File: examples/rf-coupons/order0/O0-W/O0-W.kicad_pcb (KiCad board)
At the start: 4 copper layers, 105.1 x 71.6 mm, 37 parts, among them X16 Anchor, X18 Anchor, X29 Anchor, X32 Anchor, X35 Anchor

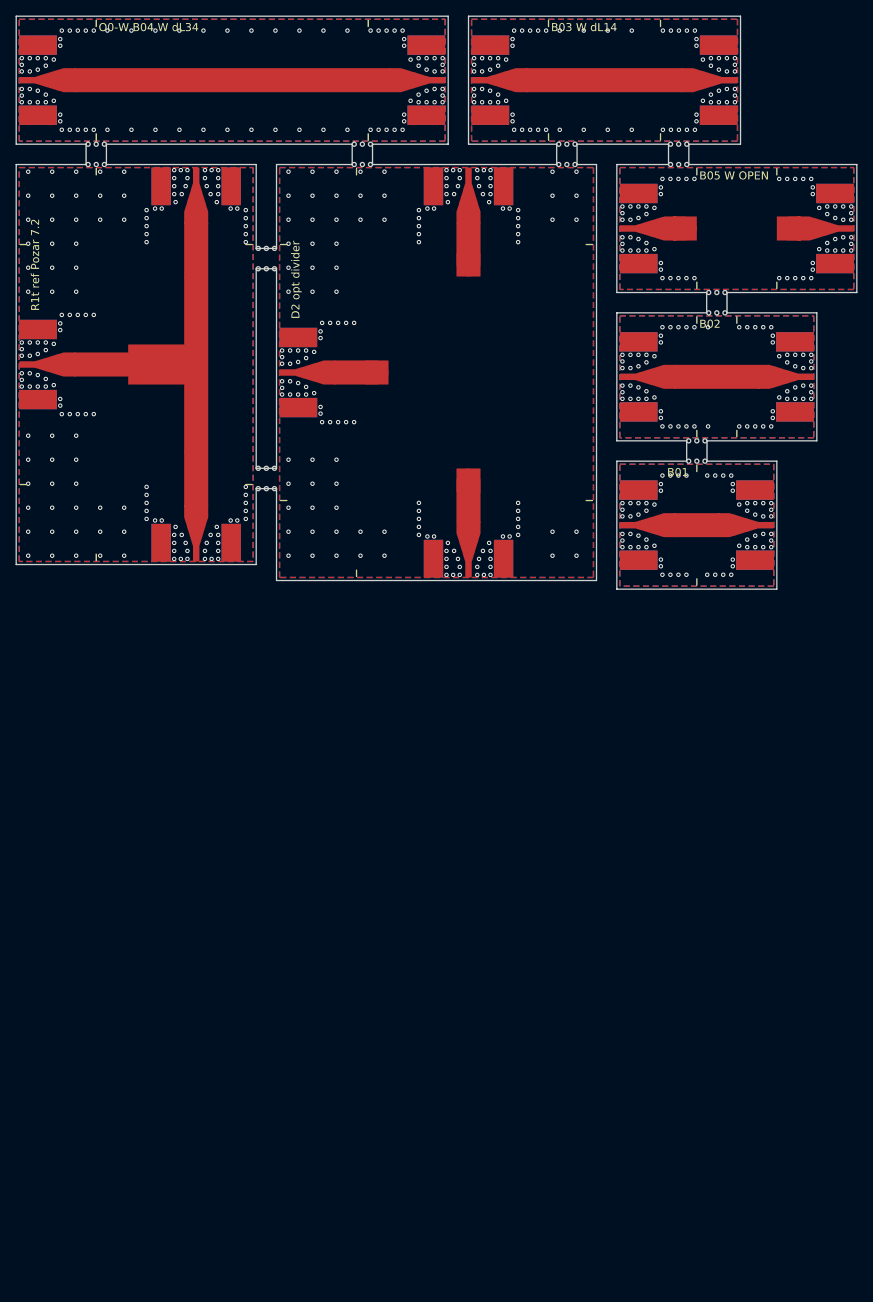
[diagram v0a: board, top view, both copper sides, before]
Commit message: Order 0: the uploads and predictions regenerated after the review
examples/rf-coupons/order0: generated from 73fe6527 (the tag carries it); KiCad
DRC under OSH Park's 4-layer rules 0 violations / 0 unconnected on all three.
`yapnr fab check` (oshpark-4l, oshpark-4l-fr408hr): O0-M 0 errors; O0-W and
O0-D stop on FAB-PLACEHOLDER until D2 and D1 are in (by design); warnings as
before (NPTH in the merged drill file; 1.511 mm of published layers):

- O0-M 120.1 x 144.3 mm, 26.9 sq in, 33 SMAs per copy, 32 tabs;
- O0-W 57.5 x 131.2 mm, 11.7 sq in, 16 SMAs, 15 tabs;
- O0-D 90.6 x 51.5 mm, 7.2 sq in, 12 SMAs, 9 tabs (A20 added).

Every stick has two or more tabs, all on edges without a launch; no plane via
under a silkscreen glyph; no mask web under 0.1 mm; the QR decodes from the
silkscreen render.

Predictions: the coupons on FR408HR and EM528 with the review's roughness
prior, the junction-corrected ring and stub (A12 notch 5.500 GHz FR408HR,
5.388 GHz EM528; A11 1.924 / 5.793 GHz), scalars.json and lines.csv. Boards A
and B regenerated (mask-opening anchors only; DRC unchanged).

docs/rf/order0: sizes and costs, R1/R1t as drawn, the renormalization to the
solver's port impedance (review H3), the C-pad method (M3), the loss basis
(M4), the scalars (L1), the sha256 rule (F9), the connector-fit pre-check, the
mask web note (L2), and the D1/D2 pages with the board around each window.

Co-Authored-By: Claude Opus 5.5 <noreply@anthropic.com>
Claude-Session: https://claude.ai/code/session_01NY8rMuBH8hTFjkoZyuqNZ7
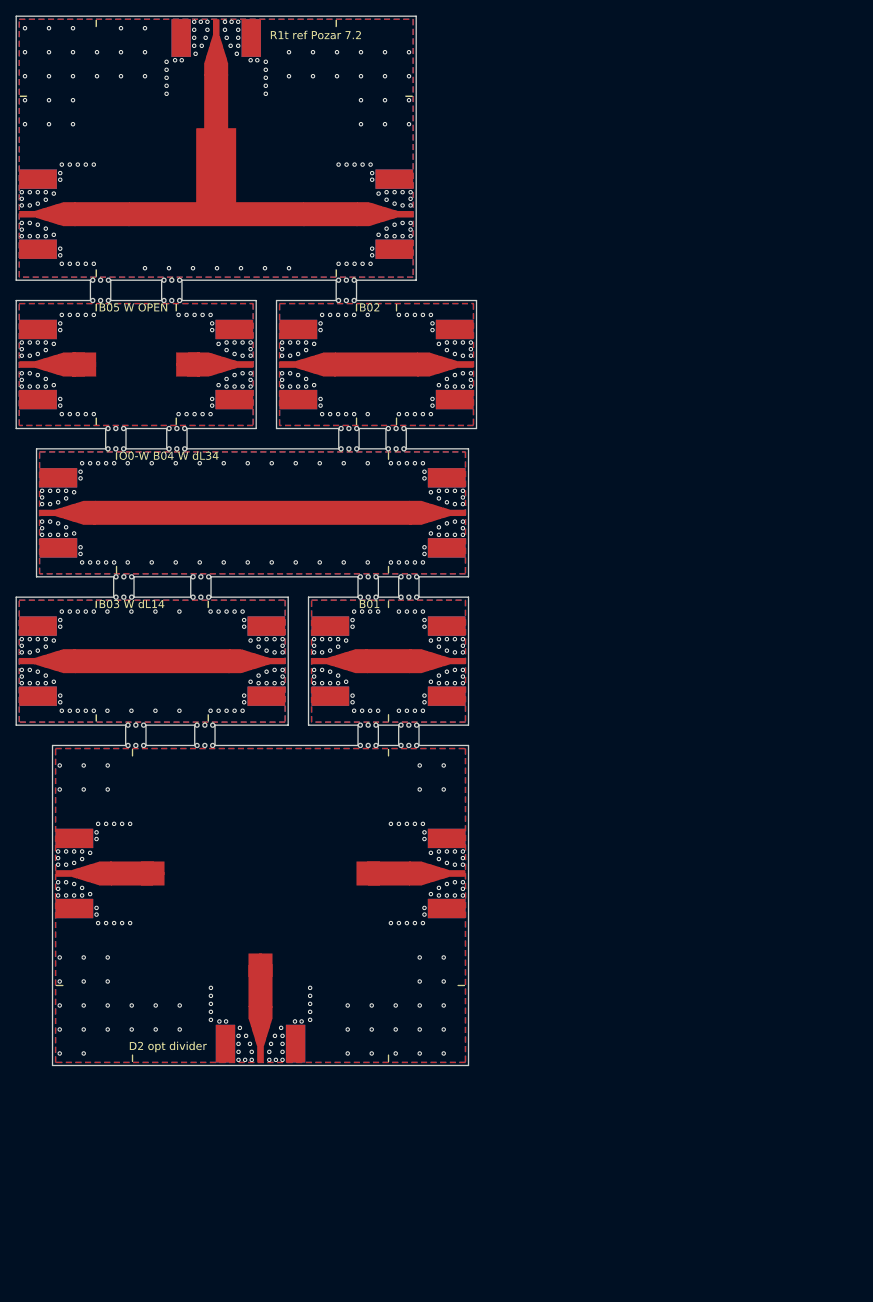
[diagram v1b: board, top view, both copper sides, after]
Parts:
- added PHD2: Placeholder_D2, Placeholder_D2, F.Cu at (50.5, 127.2)
- moved JD2_2 102.7 mm to (24.5, 127.2), turned to 0 degrees
- moved MO_B03 97.6 mm to (22.5, 94.9)
- moved MO_D2_2 92.2 mm to (27.0, 121.5)
- moved JB03E 92.0 mm to (54.0, 100.6)
- moved JB03W 92.0 mm to (20.0, 100.6)
- moved JD2_1 86.6 mm to (50.5, 151.2), turned to 90 degrees
- moved X32 85.8 mm to (37.0, 127.2), turned to 0 degrees
- moved MO_B05R 84.9 mm to (35.8, 57.8)
- moved MO_B05L 78.5 mm to (22.5, 57.8)
- moved JB05E 77.0 mm to (50.0, 63.5)
- moved JB05W 77.0 mm to (20.0, 63.5)
- moved X16 77.0 mm to (28.5, 63.5)
- moved X18 77.0 mm to (41.5, 63.5)
- moved X29 75.5 mm to (50.5, 138.7), turned to 90 degrees
- moved MO_D2_1 73.7 mm to (44.8, 137.2)
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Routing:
- net GND_D2: vias 155 -> 151
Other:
- board size 105.1 x 71.6 mm -> 57.5 x 131.2 mm
- board text added: "O0-W B01"
- board text added: "O0-W B02"
- board text added: "O0-W B03"
- board text added: "O0-W B04"
- board text added: "O0-W B05"
- board text added: "O0-W D2"
- board text added: "O0-W R1t"
- board text removed: "B03"
- board text removed: "B04"
- board text removed: "B05"
- board text removed: "D2"
- board text removed: "R1t"

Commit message: Order 0: O0-W with D2, QR label sticks, GUI-KiCad guard, pinned O0-W Gerber hash (#54)
## Summary

- **O0-W regenerated with D2** (`d2-star-sched`, compute.md's
recommendation, the pre-registered near-miss that passes |S21|/|S31| and
misses |S11| by 0.6-0.7 dB): the committed board and `catalog.json` were
still the stale placeholder predating `catalog.o_optimized`'s D2 wiring
(PR #53). KiCad DRC 0 errors / 0 warnings; `yapnr fab build` 0 errors
(headless `kicad-cli` 10.0.6).
- **A small QR label stick** (`layout_o.tag_stick`'s small-stick mode,
`catalog._label_stick`) linking each board to its docs page: O0-D's
`A15` and O0-W's `B15`, neither board had a docs link on it before (only
O0-M's own full A15 did). 25 x 25 mm, sized for a 75-char GitHub URL's
QR plus the title/stackup/git tag lines, verified with a rendered KiCad
DRC (no overlap with a neighbour).
- **GUI-KiCad guard** added to the coupons generator (`fab.kicad_cli`):
refuses a GUI `KiCad.app` (or any non-background-only app bundle) rather
than silently using it to DRC and fab-package a real OSH Park order
(DEVELOPERS.md#kicad). Self-contained, no new Bazel dependency.
- **Privacy fix**: `catalog.o_optimized` now stores a winner's footprint
path repo-relative in `catalog.json` (`islands.source`), not the
absolute machine path it was called with — found by `prek`'s privacy
scan on O0-W's first real (non-placeholder) `catalog.json` commit.
- **`preregistration.md`** records the owner's default: `d2-star-sched`
ships on O0-W as this pre-registered near-miss unless the owner says
otherwise, next to the existing "ships only as the owner decides" row,
which stays the binding text pending the owner's own sign-off.
- Panel-size regression test limits updated for the new label sticks
(O0-D 7.24 → 9.16 sq in, O0-W 11.70 → 13.28 sq in — a few extra dollars
of fab cost).

**O0-D stays the placeholder.** `d1-star`'s committed footprint still
has its two known 0.100 mm corner-gap violations (OSH Park's 0.127 mm
rule) — 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
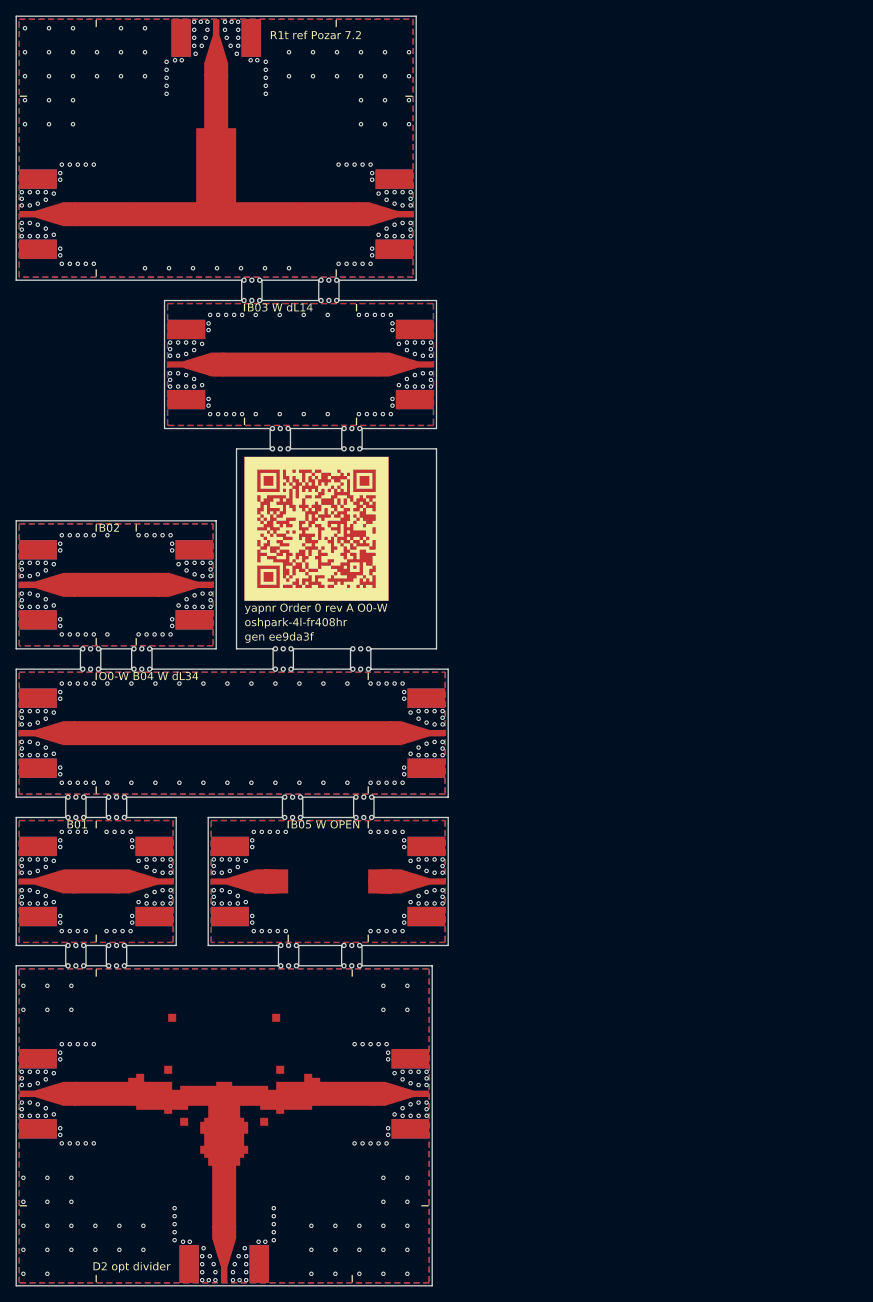
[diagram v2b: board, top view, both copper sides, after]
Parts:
- removed PHD2: Placeholder_D2, Placeholder_D2
- removed X29, X32, X35: Anchor, Anchor
- added UD2: Optimized_D2, Optimized_D2, F.Cu at (46.0, 154.7)
- moved MO_B05L 68.9 mm to (46.5, 122.5)
- moved JB05E 68.9 mm to (74.0, 128.2)
- moved JB05W 68.9 mm to (44.0, 128.2)
- moved X16 68.9 mm to (52.5, 128.2)
- moved X18 68.9 mm to (65.5, 128.2)
- moved MO_B05R 68.9 mm to (59.8, 122.5)
- moved MO_B01 45.8 mm to (22.5, 122.5)
- moved JB01E 45.8 mm to (40.0, 128.2)
- moved JB01W 45.8 mm to (20.0, 128.2)
- moved MO_B02 42.6 mm to (22.5, 85.4)
- moved JB02E 42.6 mm to (45.0, 91.1)
- moved JB02W 42.6 mm to (20.0, 91.1)
- moved MO_B03 41.5 mm to (41.0, 57.8)
- moved JB03E 41.5 mm to (72.5, 63.5)
- moved JB03W 41.5 mm to (38.5, 63.5)
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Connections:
- JD2_1 pad 1: RF_D2_1 -> RF_D2
- JD2_2 pad 1: RF_D2_2 -> RF_D2
- JD2_3 pad 1: RF_D2_3 -> RF_D2
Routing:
- net RF_D2: track 0.00 -> 19.8 mm
- net RF_D2_3: track 5.09 -> 0.00 mm
- net RF_D2_2: track 5.09 -> 0.00 mm
- net RF_D2_1: track 5.09 -> 0.00 mm
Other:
- board size 57.5 x 131.2 mm -> 54 x 158.7 mm
- board text added: "03b7d938"
- board text added: "O0-W B15"
- board text added: "gen ee9da3f"
- board text added: "oshpark-4l-fr408hr"
- board text added: "yapnr Order 0 rev A O0-W"
- board text removed: "D2 window 20 x 24"
